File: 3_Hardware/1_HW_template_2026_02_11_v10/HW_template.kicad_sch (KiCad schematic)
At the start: 20 parts, among them P1 ${SIM.PARAMS}, P2 ${SIM.PARAMS}, U1 LD1117S33TR_SOT223, U2 SiP32508, Y1 ${SIM.PARAMS}

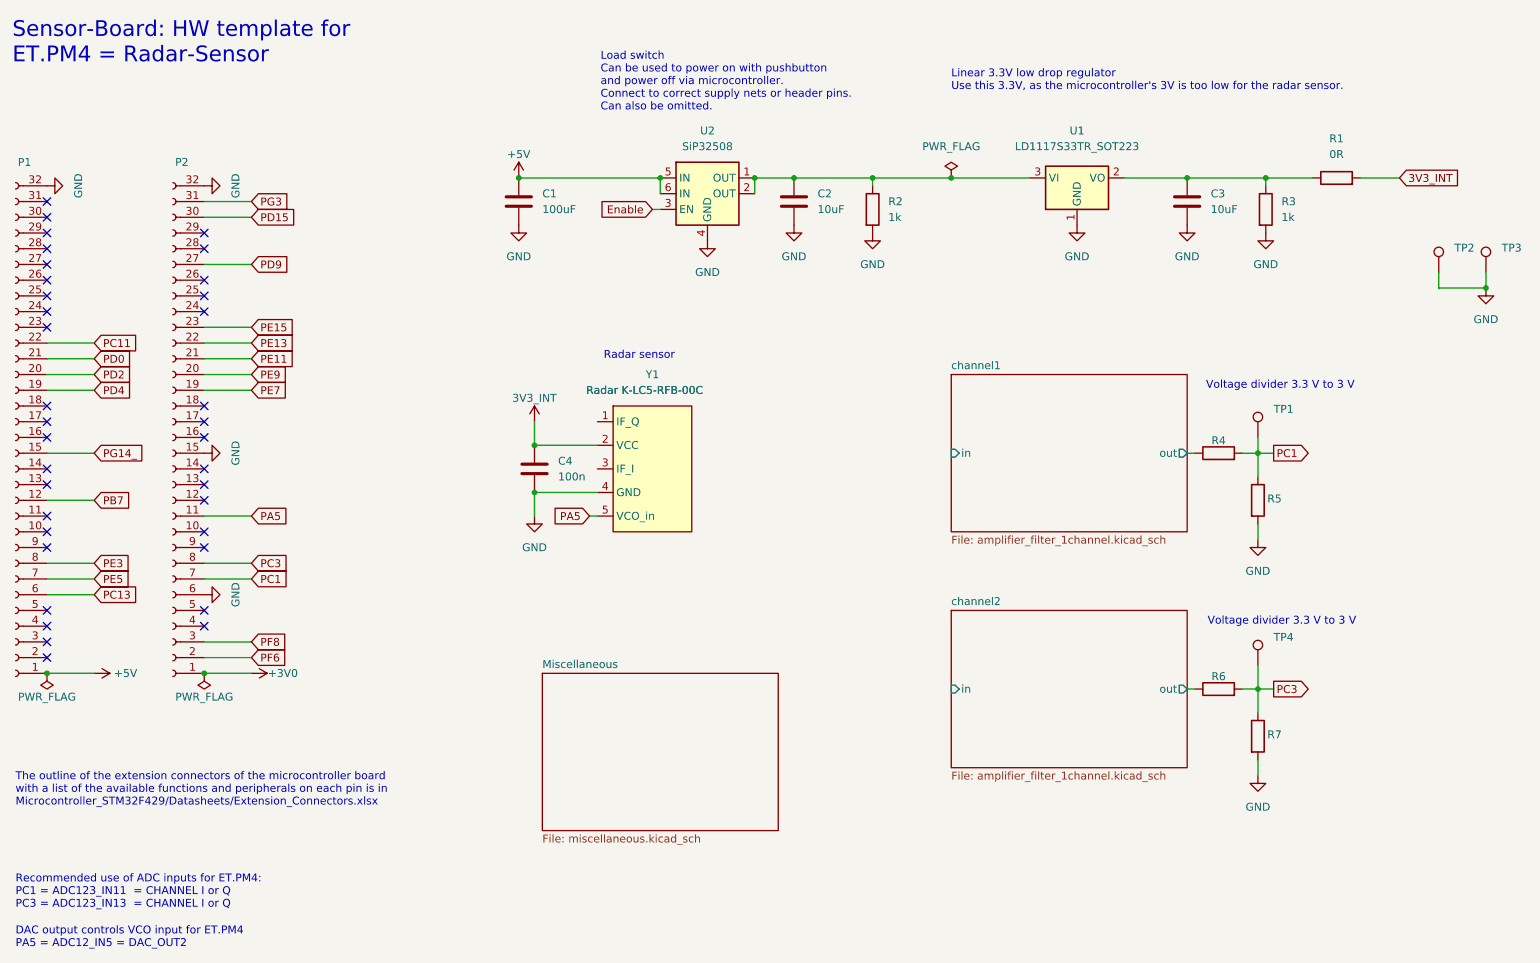
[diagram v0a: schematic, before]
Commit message: first analog circuitry implemented in kicad
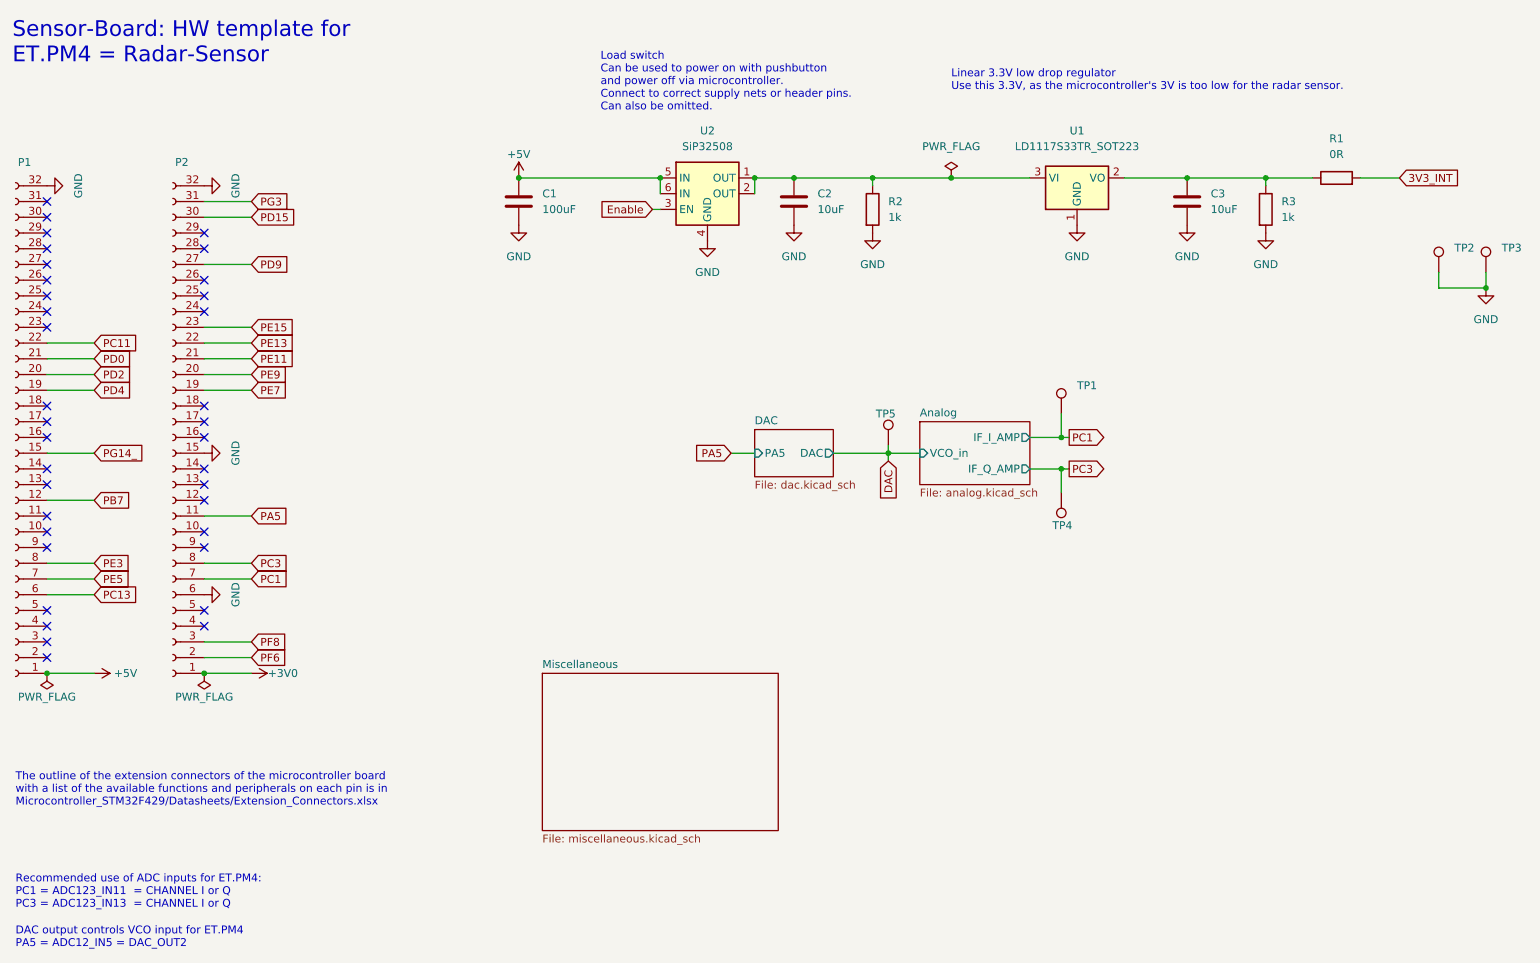
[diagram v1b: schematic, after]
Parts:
- removed C4: 100n, Capacitor_SMD:C_0805_2012Metric_Pad1.18x1.45mm_HandSolder, symbol Device:C
- removed R4, R5, R6, R7: ~, Resistor_SMD:R_0805_2012Metric_Pad1.20x1.40mm_HandSolder, symbol Device:R
- removed Y1: ${SIM.PARAMS}, HW_template:Radar_K-LC5, symbol HW_template:Radar K-LC5-RFB-00C
- added TP5: Channel1, TestPoint:TestPoint_Loop_D2.60mm_Drill1.6mm_Beaded, symbol Connector:TestPoint
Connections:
- new net DAC: TP5.1
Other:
- removed sheet channel1
- removed sheet channel2
- added sheet Analog (analog.kicad_sch)
- added sheet DAC (dac.kicad_sch)
- note removed: "Radar sensor"
- note removed: "Voltage divider 3.3 V to 3 V"
- moved on the sheet: TP1, TP4

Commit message: finalize main feature
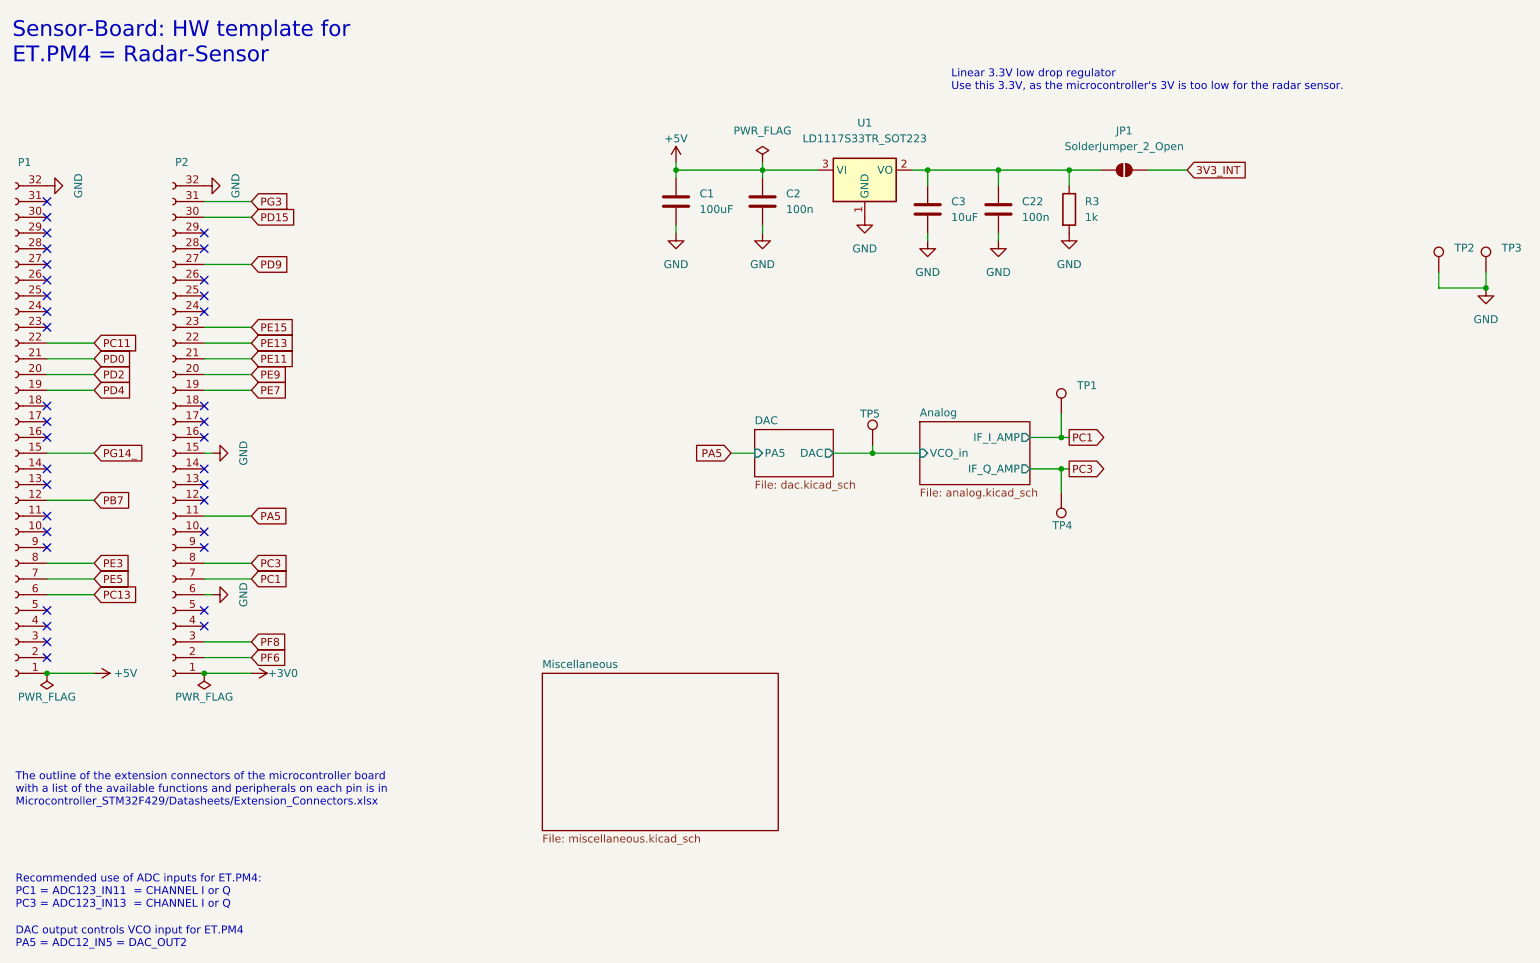
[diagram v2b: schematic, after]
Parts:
- removed R1: 0R, Resistor_SMD:R_0805_2012Metric_Pad1.20x1.40mm_HandSolder, symbol Device:R
- removed R2: 1k, Resistor_SMD:R_0805_2012Metric_Pad1.20x1.40mm_HandSolder, symbol Device:R
- removed U2: SiP32508, Package_TO_SOT_SMD:TSOT-23-6_HandSoldering, symbol HW_template:SiP32508
- added C22: 100n, Capacitor_SMD:C_0805_2012Metric_Pad1.18x1.45mm_HandSolder, symbol Device:C
- added JP1: SolderJumper_2_Open, symbol Jumper:SolderJumper_2_Open
- C2: value 10uF -> 100n
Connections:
- net +5V: now also C2.1, U1.3 (VI)
- net 3V3_INT: now also JP1.2 (B)
- net GND: now also C22.2
- net at C3.1, R3.1, U1.2 (VO): now also C22.1, JP1.1 (A)
- net DAC renamed Analog/VCO_in
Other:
- note removed: "Load switch Can be used to power on with pushbutton and power off via microcontroller. Connect to correct supply nets or header pins. Can also be omitted."
- moved on the sheet: C1, C3, R3, TP5, U1

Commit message: layout template
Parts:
- removed C1: 100uF, Capacitor_SMD:C_1206_3216Metric_Pad1.33x1.80mm_HandSolder, symbol Device:C
- removed C2, C22: 100n, Capacitor_SMD:C_0805_2012Metric_Pad1.18x1.45mm_HandSolder, symbol Device:C
- removed C3: 10uF, Capacitor_SMD:C_0805_2012Metric_Pad1.18x1.45mm_HandSolder, symbol Device:C
- removed JP1: SolderJumper_2_Open, symbol Jumper:SolderJumper_2_Open
- removed R3: 1k, Resistor_SMD:R_0805_2012Metric_Pad1.20x1.40mm_HandSolder, symbol Device:R
- removed U1: LD1117S33TR_SOT223, Package_TO_SOT_SMD:SOT-223-3_TabPin2, symbol Regulator_Linear:LD1117S33TR_SOT223
- renumbered TP5 to TP1, TP1 to TP2, TP4 to TP3, TP2 to TP4, TP3 to TP5
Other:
- added sheet power (power.kicad_sch)
- note removed: "Linear 3.3V low drop regulator Use this 3.3V, as the microcontroller's 3V is too low for the radar sensor."

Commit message: layout template
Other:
- note added: "TO BE CONNECTED TO STM"
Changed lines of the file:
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@@
 		(company "hhrt@zhaw.ch; eand@zhaw.ch")
+	)
+	(rectangle
+		(start 109.22 67.31)
+		(end 80.01 83.82)
+		(stroke
+			(width 0)
+			(type default)
+		)
+		(fill
+			(type none)
+		)
 	)
 	(text "The outline of the extension connectors of the microcontroller board\nwith a list of the available functions and peripherals on each pin is in\nMicrocontroller_STM32F429/Datasheets/Extension_Connectors.xlsx"
@@
 			)
 			(justify left bottom)
+		)
+	)
+	(text "TO BE CONNECTED TO STM\n"
+		(exclude_from_sim no)
+		(at 93.726 69.596 0)
+		(effects
+			(font
+				(size 1.27 1.27)
+			)
 		)
 	)
@@
 	(wire
 		(pts
-			(xy 93.98 72.39) (xy 96.52 72.39)
+			(xy 96.52 78.74) (xy 96.52 81.28)
 		)
 		(stroke
@@
 	(wire
 		(pts
-			(xy 93.98 64.77) (xy 96.52 64.77)
+			(xy 104.14 78.74) (xy 104.14 81.28)
 		)
 		(stroke
@@
 	(wire
 		(pts
-			(xy 93.98 68.58) (xy 96.52 68.58)
+			(xy 100.33 78.74) (xy 100.33 81.28)
 		)
 		(stroke
@@
 	(global_label "PA10"
 		(shape output)
-		(at 93.98 72.39 180)
-		(fields_autoplaced yes)
-		(effects
-			(font
-				(size 1.27 1.27)
-			)
-			(justify right)
-		)
-		(property "Intersheetrefs" "${INTERSHEET_REFS}"
-			(at 86.7893 72.3106 0)
-			(effects
-				(font
-					(size 1.27 1.27)
-				)
-				(justify right)
+		(at 96.52 78.74 90)
+		(fields_autoplaced yes)
+		(effects
+			(font
+				(size 1.27 1.27)
+			)
+			(justify left)
+		)
+		(property "Intersheetrefs" "${INTERSHEET_REFS}"
+			(at 96.52 70.9772 90)
+			(effects
+				(font
+					(size 1.27 1.27)
+				)
+				(justify left)
 				(hide yes)
 			)
@@
 	(global_label "D0"
 		(shape input)
-		(at 102.87 106.68 180)
-		(fields_autoplaced yes)
-		(effects
-			(font
-				(size 1.27 1.27)
-			)
-			(justify right)
-		)
-		(property "Intersheetrefs" "${INTERSHEET_REFS}"
-			(at 97.4053 106.68 0)
-			(effects
-				(font
-					(size 1.27 1.27)
-				)
-				(justify right)
+		(at 91.44 77.47 90)
+		(fields_autoplaced yes)
+		(effects
+			(font
+				(size 1.27 1.27)
+			)
+			(justify left)
+		)
+		(property "Intersheetrefs" "${INTERSHEET_REFS}"
+			(at 91.44 72.0053 90)
+			(effects
+				(font
+					(size 1.27 1.27)
+				)
+				(justify left)
 				(hide yes)
 			)
@@
 	(global_label "D1"
 		(shape input)
-		(at 102.87 110.49 180)
-		(fields_autoplaced yes)
-		(effects
-			(font
-				(size 1.27 1.27)
-			)
-			(justify right)
-		)
-		(property "Intersheetrefs" "${INTERSHEET_REFS}"
-			(at 97.4053 110.49 0)
-			(effects
-				(font
-					(size 1.27 1.27)
-				)
-				(justify right)
+		(at 87.63 77.47 90)
+		(fields_autoplaced yes)
+		(effects
+			(font
+				(size 1.27 1.27)
+			)
+			(justify left)
+		)
+		(property "Intersheetrefs" "${INTERSHEET_REFS}"
+			(at 87.63 72.0053 90)
+			(effects
+				(font
+					(size 1.27 1.27)
+				)
+				(justify left)
 				(hide yes)
 			)
@@
 	(global_label "PA9"
 		(shape input)
-		(at 93.98 68.58 180)
-		(fields_autoplaced yes)
-		(effects
-			(font
-				(size 1.27 1.27)
-			)
-			(justify right)
-		)
-		(property "Intersheetrefs" "${INTERSHEET_REFS}"
-			(at 87.9988 68.5006 0)
-			(effects
-				(font
-					(size 1.27 1.27)
-				)
-				(justify right)
+		(at 100.33 78.74 90)
+		(fields_autoplaced yes)
+		(effects
+			(font
+				(size 1.27 1.27)
+			)
+			(justify left)
+		)
+		(property "Intersheetrefs" "${INTERSHEET_REFS}"
+			(at 100.33 72.1867 90)
+			(effects
+				(font
+					(size 1.27 1.27)
+				)
+				(justify left)
 				(hide yes)
 			)
@@
 	(global_label "PE6"
 		(shape input)
-		(at 93.98 64.77 180)
+		(at 104.14 78.74 90)
+		(fields_autoplaced yes)
+		(effects
+			(font
+				(size 1.27 1.27)
+			)
+			(justify left)
+		)
+		(property "Intersheetrefs" "${INTERSHEET_REFS}"
+			(at 104.14 72.1263 90)
+			(effects
+				(font
+					(size 1.27 1.27)
+				)
+				(justify left)
+				(hide yes)
+			)
+		)
+	)
+	(global_label "PC3"
+		(shape input)
+		(at 63.5 109.22 0)
+		(fields_autoplaced yes)
+		(effects
+			(font
+				(size 1.27 1.27)
+			)
+			(justify left)
+		)
+		(property "Intersheetrefs" "${INTERSHEET_REFS}"
+			(at 70.2347 109.22 0)
+			(effects
+				(font
+					(size 1.27 1.27)
+				)
+				(justify left)
+				(hide yes)
+			)
+		)
+	)
+	(global_label "PC13"
+		(shape input)
+		(at 38.1 114.3 0)
+		(fields_autoplaced yes)
+		(effects
+			(font
+				(size 1.27 1.27)
+			)
+			(justify left)
+		)
+		(property "Intersheetrefs" "${INTERSHEET_REFS}"
+			(at 45.4721 114.3794 0)
+			(effects
+				(font
+					(size 1.27 1.27)
+				)
+				(justify left)
+				(hide yes)
+			)
+		)
+	)
+	(global_label "PA5"
+		(shape input)
+		(at 140.97 91.44 180)
 		(fields_autoplaced yes)
 		(effects
@@
 		)
 		(property "Intersheetrefs" "${INTERSHEET_REFS}"
-			(at 87.9383 64.6906 0)
+			(at 134.4167 91.44 0)
 			(effects
 				(font
@@
 		)
 	)
-	(global_label "PC3"
-		(shape input)
-		(at 63.5 109.22 0)
-		(fields_autoplaced yes)
-		(effects
-			(font
-				(size 1.27 1.27)
-			)
-			(justify left)
-		)
-		(property "Intersheetrefs" "${INTERSHEET_REFS}"
-			(at 70.2347 109.22 0)
-			(effects
-				(font
-					(size 1.27 1.27)
-				)
-				(justify left)
-				(hide yes)
-			)
-		)
-	)
-	(global_label "PC13"
-		(shape input)
-		(at 38.1 114.3 0)
-		(fields_autoplaced yes)
-		(effects
-			(font
-				(size 1.27 1.27)
-			)
-			(justify left)
-		)
-		(property "Intersheetrefs" "${INTERSHEET_REFS}"
-			(at 45.4721 114.3794 0)
-			(effects
-				(font
-					(size 1.27 1.27)
-				)
-				(justify left)
-				(hide yes)
-			)
-		)
-	)
-	(global_label "PA5"
-		(shape input)
-		(at 140.97 91.44 180)
-		(fields_autoplaced yes)
-		(effects
-			(font
-				(size 1.27 1.27)
-			)
-			(justify right)
-		)
-		(property "Intersheetrefs" "${INTERSHEET_REFS}"
-			(at 134.4167 91.44 0)
-			(effects
-				(font
-					(size 1.27 1.27)
-				)
-				(justify right)
-				(hide yes)
-			)
-		)
-	)
 	(global_label "Buzz"
 		(shape input)
-		(at 101.6 115.57 180)
-		(fields_autoplaced yes)
-		(effects
-			(font
-				(size 1.27 1.27)
-			)
-			(justify right)
-		)
-		(property "Intersheetrefs" "${INTERSHEET_REFS}"
-			(at 94.1396 115.57 0)
-			(effects
-				(font
-					(size 1.27 1.27)
-				)
-				(justify right)
-				(hide yes)
-			)
+		(at 83.82 78.74 90)
+		(fields_autoplaced yes)
+		(effects
+			(font
+				(size 1.27 1.27)
+			)
+			(justify left)
+		)
+		(property "Intersheetrefs" "${INTERSHEET_REFS}"
+			(at 83.82 71.2796 90)
+			(effects
+				(font
+					(size 1.27 1.27)
+				)
+				(justify left)
+				(hide yes)
+			)

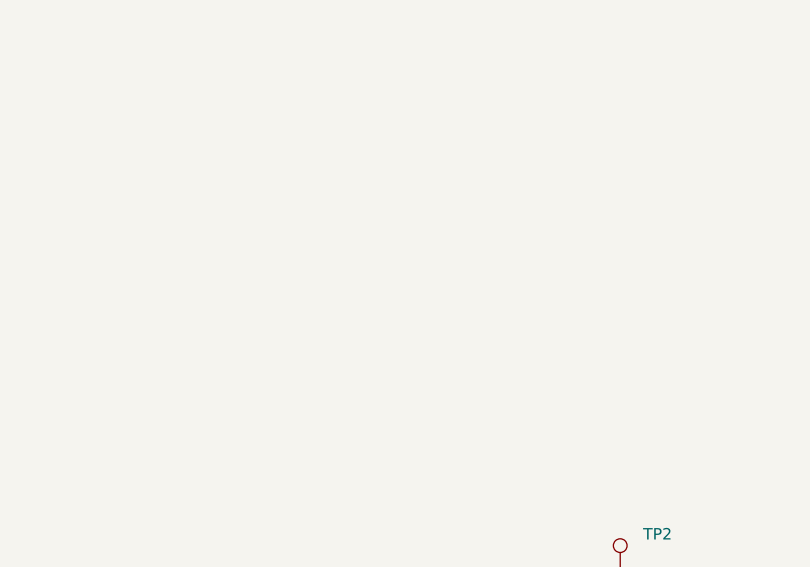
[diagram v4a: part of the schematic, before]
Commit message: added ecg schematic and part list to order
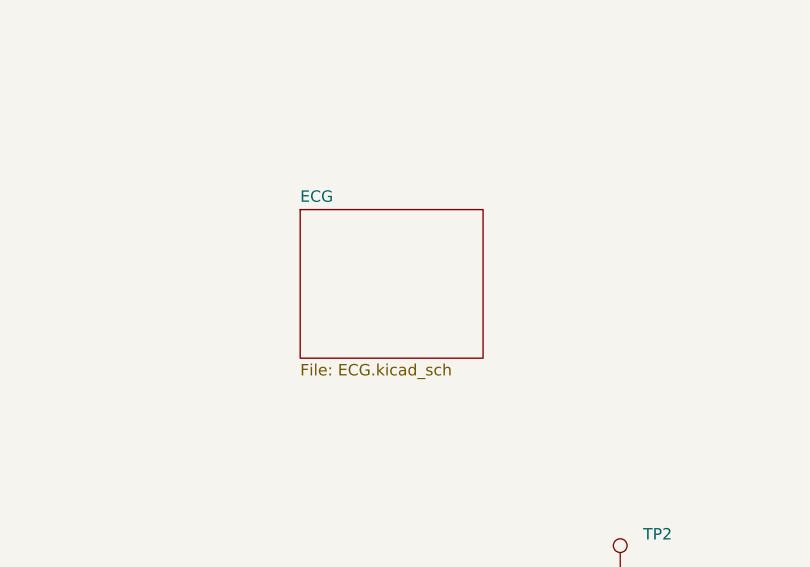
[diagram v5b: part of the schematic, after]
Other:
- added sheet ECG (ECG.kicad_sch)
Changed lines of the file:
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@@
+	)
+	(sheet
+		(at 158.75 44.45)
+		(size 20.32 16.51)
+		(exclude_from_sim no)
+		(in_bom yes)
+		(on_board yes)
+		(dnp no)
+		(fields_autoplaced yes)
+		(stroke
+			(width 0.1524)
+			(type solid)
+		)
+		(fill
+			(color 0 0 0 0.0000)
+		)
+		(property "Sheetname" "ECG"
+			(at 158.75 43.7384 0)
+			(effects
+				(font
+					(size 1.27 1.27)
+				)
+				(justify left bottom)
+			)
+		)
+		(property "Sheetfile" "ECG.kicad_sch"
+			(at 158.75 61.5446 0)
+			(effects
+				(font
+					(size 1.27 1.27)
+				)
+				(justify left top)
+			)
+		)
+		(instances
+			(project "HW_template"
+				(path "/1f276d59-ad9b-4e70-a842-f3b7e562eb9b"
+					(page "8")
+				)
+			)
+		)
 	)
 	(sheet

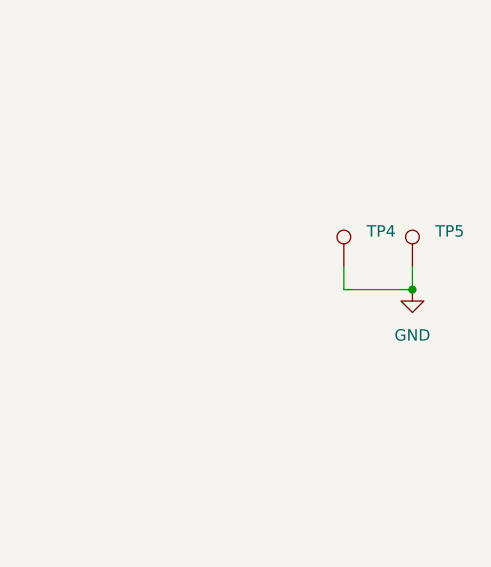
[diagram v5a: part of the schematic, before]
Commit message: updated layout
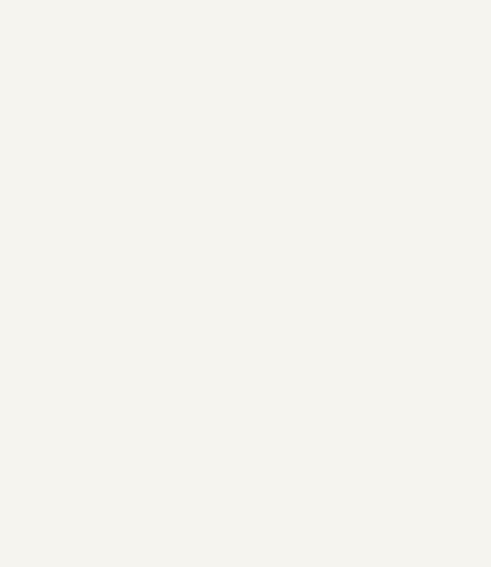
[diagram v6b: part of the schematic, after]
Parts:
- removed TP4, TP5: ${SIM.PARAMS}, TestPoint:TestPoint_Loop_D2.60mm_Drill1.6mm_Beaded, symbol Connector:TestPoint
